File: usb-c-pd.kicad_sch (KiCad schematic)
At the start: 17 parts, among them J10 Conn_01x04_Pin, J11 USB_C_Receptacle_USB2.0_16P, J12 Conn_01x03_Pin, Q4 AO3400A, U6 IP2721

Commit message: switch to cheaper components.
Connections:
- net +VSUB renamed VBUS
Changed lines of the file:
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@@
+	)
+	(symbol
+		(lib_id "power:VBUS")
+		(at 57.15 43.18 0)
+		(unit 1)
+		(exclude_from_sim no)
+		(in_bom yes)
+		(on_board yes)
+		(dnp no)
+		(fields_autoplaced yes)
+		(property "Reference" "#PWR02"
+			(at 57.15 46.99 0)
+			(effects
+				(font
+					(size 1.27 1.27)
+				)
+				(hide yes)
+			)
+		)
+		(property "Value" "VBUS"
+			(at 57.15 38.1 0)
+			(effects
+				(font
+					(size 1.27 1.27)
+				)
+			)
+		)
+		(property "Footprint" ""
+			(at 57.15 43.18 0)
+			(effects
+				(font
+					(size 1.27 1.27)
+				)
+				(hide yes)
+			)
+		)
+		(property "Datasheet" ""
+			(at 57.15 43.18 0)
+			(effects
+				(font
+					(size 1.27 1.27)
+				)
+				(hide yes)
+			)
+		)
+		(property "Description" "Power symbol creates a global label with name \"VBUS\""
+			(at 57.15 43.18 0)
+			(effects
+				(font
+					(size 1.27 1.27)
+				)
+				(hide yes)
+			)
+		)
+		(pin "1"
+		)
+		(instances
+			(project "dmx"
+				(path "/860489ce-8e24-49a4-b6b1-5a2692123cd9/9b64c4ee-de50-4174-a7da-382288dc1185"
+					(reference "#PWR02")
+					(unit 1)
+				)
+			)
+		)
 	)
 	(symbol
@@
 					(unit 1)
 				)
-			)
-		)
-	)
-	(symbol
-		(lib_id "+VUSB:+VSUB")
-		(at 57.15 43.18 0)
-		(unit 1)
-		(exclude_from_sim no)
-		(in_bom no)
-		(on_board no)
-		(dnp no)
-		(fields_autoplaced yes)
-		(property "Reference" "#+VUSB01"
-			(at 58.42 40.6399 0)
-			(effects
-				(font
-					(size 1.27 1.27)
-				)
-				(justify left)
-			)
-		)
-		(property "Value" "+VSUB"
-			(at 65.024 44.45 0)
-			(effects
-				(font
-					(size 1.27 1.27)
-				)
-				(hide yes)
-			)
-		)
-		(property "Footprint" ""
-			(at 57.15 43.18 0)
-			(effects
-				(font
-					(size 1.27 1.27)
-				)
-				(hide yes)
-			)
-		)
-		(property "Datasheet" ""
-			(at 57.15 43.18 0)
-			(effects
-				(font
-					(size 1.27 1.27)
-				)
-				(hide yes)
-			)
-		)
-		(property "Description" ""
-			(at 57.15 43.18 0)
-			(effects
-				(font
-					(size 1.27 1.27)
-				)
-				(hide yes)
-			)
-		)
-		(pin "1"
-		)
-		(instances
-			(project "dmx"
-				(path "/860489ce-8e24-49a4-b6b1-5a2692123cd9/9b64c4ee-de50-4174-a7da-382288dc1185"
-					(reference "#+VUSB01")
-					(unit 1)
-				)

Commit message: replace extended components with basic components.
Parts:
- J11: footprint Connector_USB:USB_C_Receptacle_G-Switch_GT-USB-7010ASV -> USB-C-Power-tester:TYPE-C-31-M-12; LCSC C2988369 -> C165948
- R61, R62: extended (none) -> optional
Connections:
- no-connect marks 0 -> 6
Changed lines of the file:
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@@
+	)
+	(junction
+		(at 55.88 45.72)
+		(diameter 0)
+		(color 0 0 0 0)
 	)
 	(junction
@@
 		(color 0 0 0 0)
 	)
+	(no_connect
+		(at 55.88 72.39)
+	)
+	(no_connect
+		(at 55.88 90.17)
+	)
+	(no_connect
+		(at 55.88 80.01)
+	)
+	(no_connect
+		(at 55.88 87.63)
+	)
+	(no_connect
+		(at 55.88 77.47)
+	)
+	(no_connect
+		(at 55.88 74.93)
+	)
 	(wire
 		(pts
@@
 	(wire
 		(pts
+			(xy 55.88 45.72) (xy 55.88 43.18)
+		)
+		(stroke
+			(width 0)
+			(type default)
+		)
+	)
+	(wire
+		(pts
 			(xy 93.98 78.74) (xy 93.98 97.79)
 		)
@@
 	(wire
 		(pts
-			(xy 55.88 59.69) (xy 55.88 43.18)
+			(xy 55.88 59.69) (xy 55.88 45.72)
 		)
 		(stroke
@@
 			)
 		)
+		(property "extended" "optional"
+			(at 77.47 77.47 0)
+			(effects
+				(font
+					(size 1.27 1.27)
+				)
+				(hide yes)
+			)
+		)
 		(pin "1"
 		)
@@
 			)
 		)
+		(property "extended" "optional"
+			(at 175.26 54.61 0)
+			(effects
+				(font
+					(size 1.27 1.27)
+				)
+				(hide yes)
+			)
+		)
 		(pin "1"
 		)
@@
 			)
 		)
-		(property "Footprint" "Connector_USB:USB_C_Receptacle_G-Switch_GT-USB-7010ASV"
+		(property "Footprint" "USB-C-Power-tester:TYPE-C-31-M-12"
 			(at 44.45 74.93 0)
 			(effects
@@
 			)
 		)
-		(property "LCSC" "C2988369"
+		(property "LCSC" "C165948"
 			(at 40.64 74.93 0)
 			(effects
@@
 					(unit 1)
 				)
+			)
+		)
+	)
+	(symbol
+		(lib_id "power:PWR_FLAG")
+		(at 55.88 45.72 90)
+		(unit 1)
+		(exclude_from_sim no)
+		(in_bom yes)
+		(on_board yes)
+		(dnp no)
+		(fields_autoplaced yes)
+		(property "Reference" "#FLG02"
+			(at 53.975 45.72 0)
+			(effects
+				(font
+					(size 1.27 1.27)
+				)
+				(hide yes)
+			)
+		)
+		(property "Value" "PWR_FLAG"
+			(at 52.07 45.7199 90)
+			(effects
+				(font
+					(size 1.27 1.27)
+				)
+				(justify left)
+			)
+		)
+		(property "Footprint" ""
+			(at 55.88 45.72 0)
+			(effects
+				(font
+					(size 1.27 1.27)
+				)
+				(hide yes)
+			)
+		)
+		(property "Datasheet" "~"
+			(at 55.88 45.72 0)
+			(effects
+				(font
+					(size 1.27 1.27)
+				)
+				(hide yes)
+			)
+		)
+		(property "Description" "Special symbol for telling ERC where power comes from"
+			(at 55.88 45.72 0)
+			(effects
+				(font
+					(size 1.27 1.27)
+				)
+				(hide yes)
+			)
+		)
+		(pin "1"
+		)
+		(instances
+			(project "dmx"
+				(path "/860489ce-8e24-49a4-b6b1-5a2692123cd9/9b64c4ee-de50-4174-a7da-382288dc1185"
+					(reference "#FLG02")
+					(unit 1)
+				)

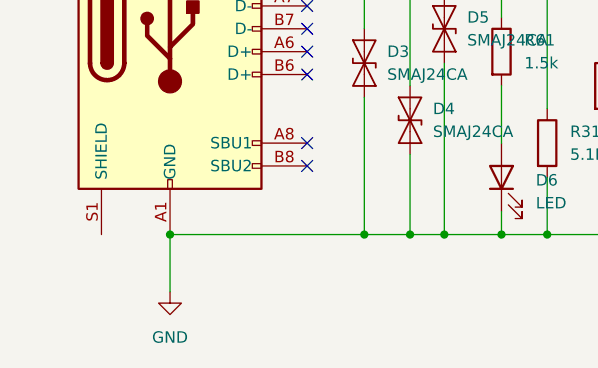
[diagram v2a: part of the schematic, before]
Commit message: add a +5V bridge to disbale the arduino
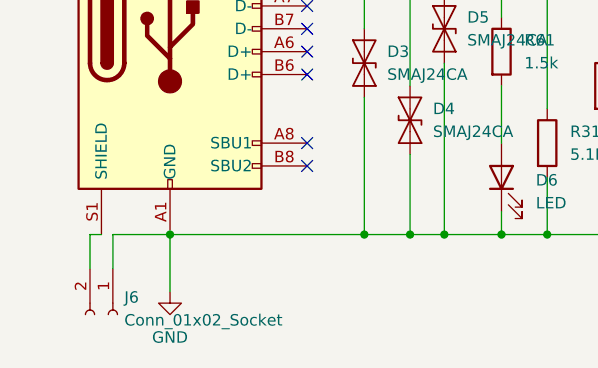
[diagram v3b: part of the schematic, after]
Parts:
- added J6: Conn_01x02_Socket, Connector_PinSocket_2.54mm:PinSocket_1x02_P2.54mm_Vertical, symbol Connector:Conn_01x02_Socket
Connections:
- net GND: now also J6.1 (Pin_1)
- net at J11.S1 (SHIELD): now also J6.2 (Pin_2)
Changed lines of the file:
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@@
+	(wire
+		(pts
+			(xy 31.75 97.79) (xy 31.75 101.6)
+		)
+		(stroke
+			(width 0)
+			(type default)
+		)
+	)
 	(wire
 		(pts
@@
 	(wire
 		(pts
+			(xy 34.29 97.79) (xy 40.64 97.79)
+		)
+		(stroke
+			(width 0)
+			(type default)
+		)
+	)
+	(wire
+		(pts
 			(xy 40.64 97.79) (xy 40.64 104.14)
 		)
@@
 	(wire
 		(pts
+			(xy 33.02 97.79) (xy 31.75 97.79)
+		)
+		(stroke
+			(width 0)
+			(type default)
+		)
+	)
+	(wire
+		(pts
 			(xy 93.98 59.69) (xy 93.98 71.12)
 		)
@@
 		(pts
 			(xy 62.23 97.79) (xy 67.31 97.79)
+		)
+		(stroke
+			(width 0)
+			(type default)
+		)
+	)
+	(wire
+		(pts
+			(xy 34.29 101.6) (xy 34.29 97.79)
 		)
 		(stroke
@@
 		)
 	)
+	(symbol
+		(lib_id "Connector:Conn_01x02_Socket")
+		(at 34.29 106.68 270)
+		(unit 1)
+		(exclude_from_sim no)
+		(in_bom yes)
+		(on_board yes)
+		(dnp no)
+		(fields_autoplaced yes)
+		(property "Reference" "J6"
+			(at 35.56 104.7749 90)
+			(effects
+				(font
+					(size 1.27 1.27)
+				)
+				(justify left)
+			)
+		)
+		(property "Value" "Conn_01x02_Socket"
+			(at 35.56 107.3149 90)
+			(effects
+				(font
+					(size 1.27 1.27)
+				)
+				(justify left)
+			)
+		)
+		(property "Footprint" "Connector_PinSocket_2.54mm:PinSocket_1x02_P2.54mm_Vertical"
+			(at 34.29 106.68 0)
+			(effects
+				(font
+					(size 1.27 1.27)
+				)
+				(hide yes)
+			)
+		)
+		(property "Datasheet" "~"
+			(at 34.29 106.68 0)
+			(effects
+				(font
+					(size 1.27 1.27)
+				)
+				(hide yes)
+			)
+		)
+		(property "Description" "Generic connector, single row, 01x02, script generated"
+			(at 34.29 106.68 0)
+			(effects
+				(font
+					(size 1.27 1.27)
+				)
+				(hide yes)
+			)
+		)
+		(pin "1"
+		)
+		(pin "2"
+		)
+		(instances
+			(project "dmx"
+				(path "/860489ce-8e24-49a4-b6b1-5a2692123cd9/9b64c4ee-de50-4174-a7da-382288dc1185"
+					(reference "J6")
+					(unit 1)
+				)
+			)
+		)
+	)

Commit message: change some last parts.
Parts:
- Q4: LCSC (none) -> C20917
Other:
- moved on the sheet: C1
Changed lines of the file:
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@@
 	(wire
 		(pts
-			(xy 167.64 58.42) (xy 167.64 46.99)
+			(xy 167.64 72.39) (xy 167.64 46.99)
 		)
 		(stroke
@@
 	(wire
 		(pts
-			(xy 167.64 66.04) (xy 167.64 97.79)
+			(xy 167.64 80.01) (xy 167.64 97.79)
 		)
 		(stroke
@@
 	(symbol
 		(lib_id "Device:C")
-		(at 167.64 62.23 0)
+		(at 167.64 76.2 0)
 		(unit 1)
 		(exclude_from_sim no)
@@
 		(dnp no)
 		(property "Reference" "C1"
-			(at 171.45 60.9599 0)
+			(at 171.45 74.9299 0)
 			(effects
 				(font
@@
 		)
 		(property "Value" "10uF"
-			(at 171.45 63.4999 0)
+			(at 171.45 77.4699 0)
 			(effects
 				(font
@@
 		)
 		(property "Footprint" "Capacitor_SMD:C_0603_1608Metric"
-			(at 168.6052 66.04 0)
+			(at 168.6052 80.01 0)
 			(effects
 				(font
@@
 		)
 		(property "Datasheet" "~"
-			(at 167.64 62.23 0)
+			(at 167.64 76.2 0)
 			(effects
 				(font
@@
 		)
 		(property "Description" "Unpolarized capacitor"
-			(at 167.64 62.23 0)
+			(at 167.64 76.2 0)
 			(effects
 				(font
@@
 			(effects
 				(font
+					(size 1.27 1.27)
+				)
+				(hide yes)
+			)
+		)
+		(property "LCSC" "C20917"
+			(at 151.13 49.53 90)
+			(effects
+				(font
